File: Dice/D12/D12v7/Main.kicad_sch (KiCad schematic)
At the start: 29 parts, among them J1 Conn_01x14, J2 Conn_01x04, J4 DNP, U1 N52810_QFN32, U2 SC7A20HTR, U5 BL24C02F-NTRC, U8 SL1605, Y1 32MHz 40ppm

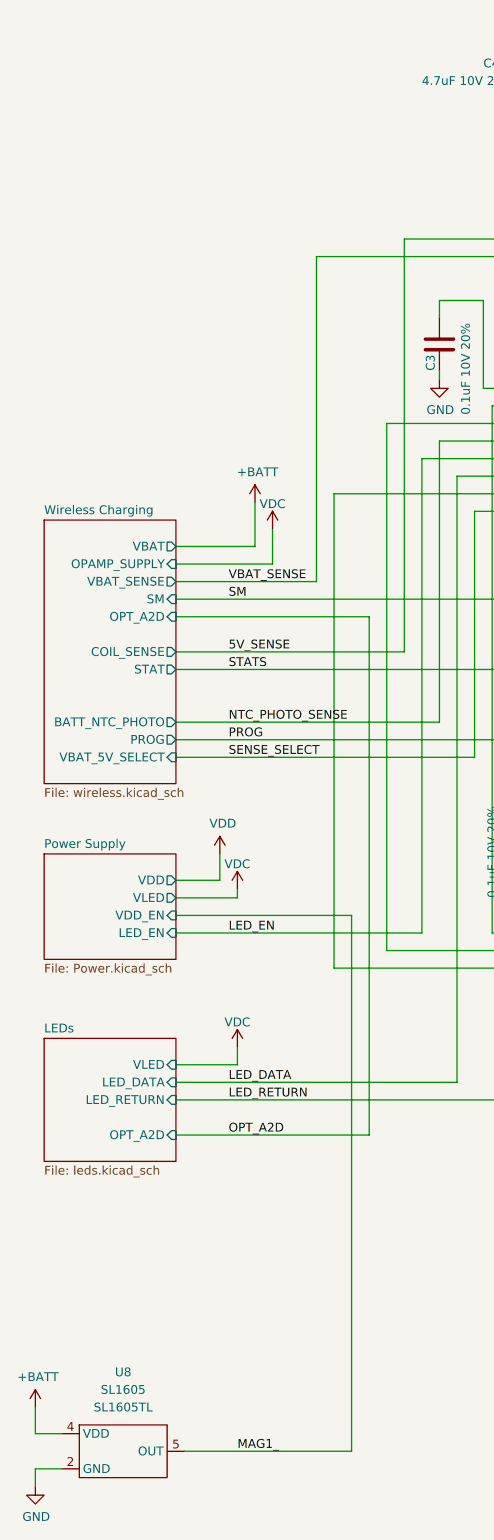
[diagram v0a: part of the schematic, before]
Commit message: Updated schematic Titles in D20V17 and likes, added 12mm D6 and Charging Jig
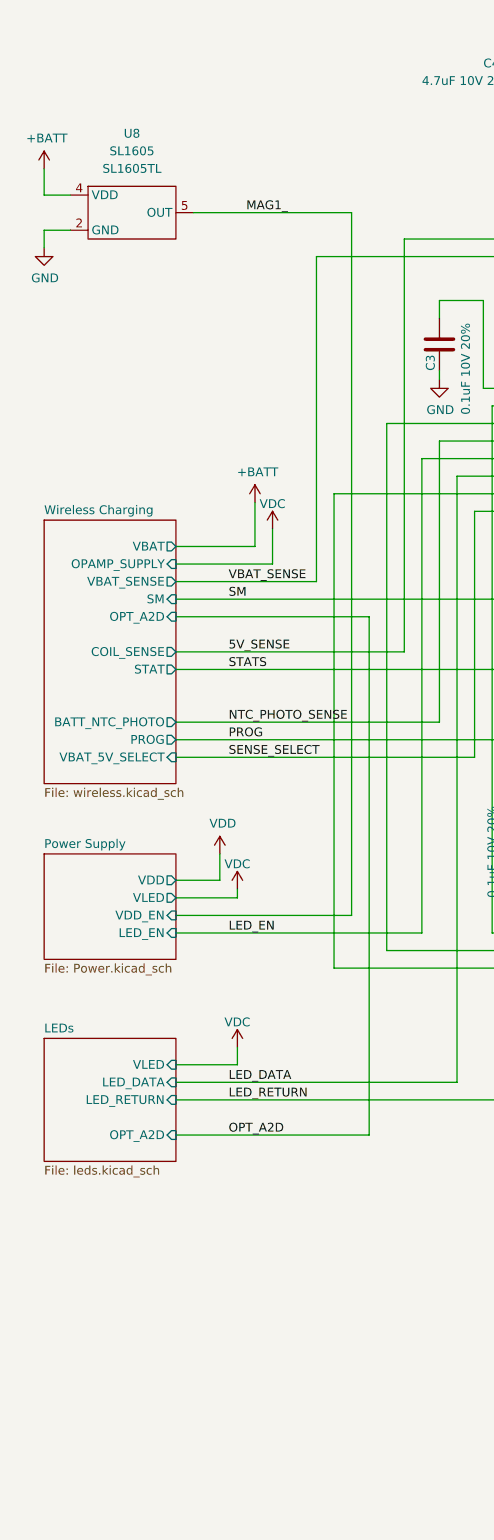
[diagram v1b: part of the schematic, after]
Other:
- title: Pixels D20 Schematic, Main -> Pixels D12 Schematic, Main
- moved on the sheet: U8
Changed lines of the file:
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@@
 	(paper "A4")
 	(title_block
-		(title "Pixels D20 Schematic, Main")
-		(date "2022-08-26")
+		(title "Pixels D12 Schematic, Main")
+		(date "2025-10-10")
 		(rev "13")
 		(company "Systemic Games, LLC")
@@
 	(wire
 		(pts
-			(xy 40.64 227.33) (xy 64.77 227.33)
+			(xy 41.91 48.26) (xy 64.77 48.26)
 		)
 		(stroke
@@
 	(wire
 		(pts
-			(xy 19.05 220.98) (xy 19.05 224.79)
+			(xy 20.32 41.91) (xy 20.32 45.72)
 		)
 		(stroke
@@
 	(wire
 		(pts
-			(xy 64.77 149.86) (xy 64.77 227.33)
+			(xy 64.77 149.86) (xy 64.77 48.26)
 		)
 		(stroke
@@
 	(wire
 		(pts
-			(xy 22.86 229.87) (xy 19.05 229.87)
+			(xy 24.13 50.8) (xy 20.32 50.8)
 		)
 		(stroke
@@
 	(wire
 		(pts
-			(xy 19.05 229.87) (xy 19.05 232.41)
+			(xy 20.32 50.8) (xy 20.32 53.34)
 		)
 		(stroke
@@
 	(wire
 		(pts
-			(xy 19.05 224.79) (xy 22.86 224.79)
+			(xy 20.32 45.72) (xy 24.13 45.72)
 		)
 		(stroke
@@
 	)
 	(label "MAG1_"
-		(at 48.26 227.33 0)
+		(at 49.53 48.26 0)
 		(effects
 			(font
@@
 	(symbol
 		(lib_id "power:GND")
-		(at 19.05 232.41 0)
+		(at 20.32 53.34 0)
 		(unit 1)
 		(exclude_from_sim no)
@@
 		(dnp no)
 		(property "Reference" "#PWR045"
-			(at 19.05 238.76 0)
+			(at 20.32 59.69 0)
 			(effects
 				(font
@@
 		)
 		(property "Value" "GND"
-			(at 19.177 236.8042 0)
+			(at 20.447 57.7342 0)
 			(effects
 				(font
@@
 		)
 		(property "Footprint" ""
-			(at 19.05 232.41 0)
+			(at 20.32 53.34 0)
 			(effects
 				(font
@@
 		)
 		(property "Datasheet" ""
-			(at 19.05 232.41 0)
+			(at 20.32 53.34 0)
 			(effects
 				(font
@@
 		)
 		(property "Description" ""
-			(at 19.05 232.41 0)
+			(at 20.32 53.34 0)
 			(effects
 				(font
@@
 	(symbol
 		(lib_id "power:+BATT")
-		(at 19.05 220.98 0)
+		(at 20.32 41.91 0)
 		(unit 1)
 		(exclude_from_sim no)
@@
 		(dnp no)
 		(property "Reference" "#PWR017"
-			(at 19.05 224.79 0)
+			(at 20.32 45.72 0)
 			(effects
 				(font
@@
 		)
 		(property "Value" "+BATT"
-			(at 19.431 216.5858 0)
+			(at 20.701 37.5158 0)
 			(effects
 				(font
@@
 		)
 		(property "Footprint" ""
-			(at 19.05 220.98 0)
+			(at 20.32 41.91 0)
 			(effects
 				(font
@@
 		)
 		(property "Datasheet" ""
-			(at 19.05 220.98 0)
+			(at 20.32 41.91 0)
 			(effects
 				(font
@@
 		)
 		(property "Description" ""
-			(at 19.05 220.98 0)
+			(at 20.32 41.91 0)
 			(effects
 				(font
@@
 	(symbol
 		(lib_id "Pixels-dice:SL1605")
-		(at 31.75 227.33 0)
+		(at 33.02 48.26 0)
 		(unit 1)
 		(exclude_from_sim no)
@@
 		(fields_autoplaced yes)
 		(property "Reference" "U8"
-			(at 31.75 215.9 0)
+			(at 33.02 36.83 0)
 			(effects
 				(font
@@
 		)
 		(property "Value" "SL1605"
-			(at 31.75 218.44 0)
+			(at 33.02 39.37 0)
 			(effects
 				(font
@@
 		)
 		(property "Footprint" "Package_TO_SOT_SMD:SOT-553"
-			(at 31.75 227.33 0)
+			(at 33.02 48.26 0)
 			(effects
 				(font
@@
 		)
 		(property "Datasheet" ""
-			(at 31.75 227.33 0)
+			(at 33.02 48.26 0)
 			(effects
 				(font
@@
 		)
 		(property "Description" ""
-			(at 31.75 227.33 0)
+			(at 33.02 48.26 0)
 			(effects
 				(font
@@
 		)
 		(property "Manufacturer" "Slkor(SLKORMICRO Elec.)"
-			(at 31.75 227.33 0)
+			(at 33.02 48.26 0)
 			(effects
 				(font
@@
 		)
 		(property "Part Number" "SL1605TL"
-			(at 31.75 220.98 0)
+			(at 33.02 41.91 0)
 			(effects
 				(font
@@
 		)
 		(property "LCSC Part #" "C2826474"
-			(at 31.75 227.33 0)
+			(at 33.02 48.26 0)
 			(effects
 				(font
